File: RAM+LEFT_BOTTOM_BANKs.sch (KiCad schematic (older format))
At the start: 12 parts, among them U301 iCE40-HX4K-TQ144, U501 AS4C1M16S

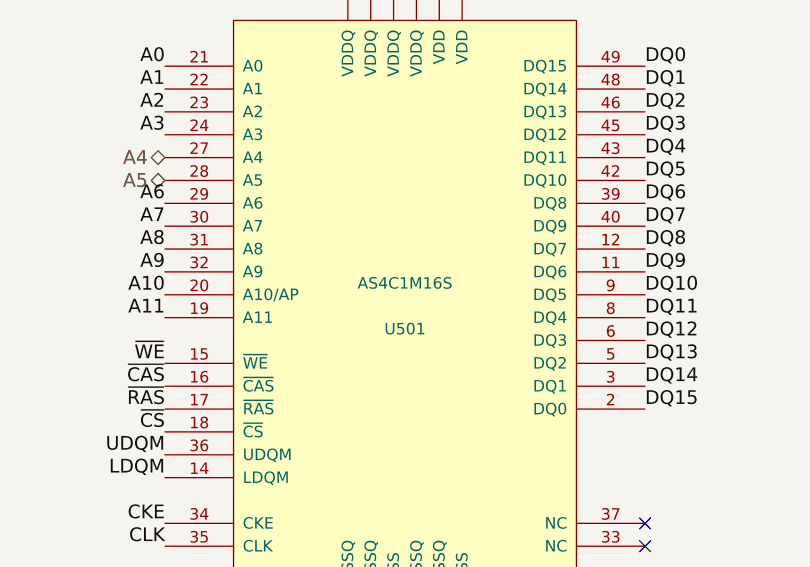
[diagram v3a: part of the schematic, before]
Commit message: Renamed PN: AS4C1M16S->AS4C1M16S-7TCN; MIC5270->MIC5270-3.0YM5-TR; CLC4007->CLC4007ITP14MTR
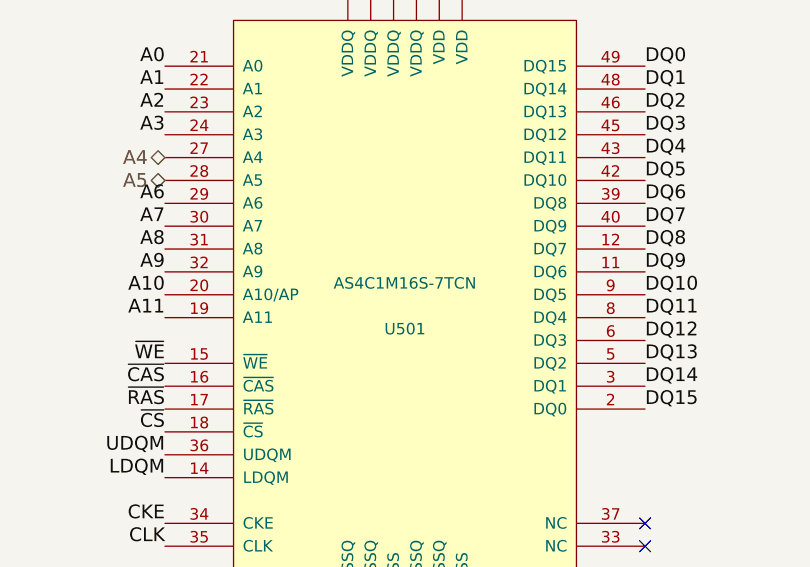
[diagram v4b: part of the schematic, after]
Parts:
- U501: value AS4C1M16S -> AS4C1M16S-7TCN
